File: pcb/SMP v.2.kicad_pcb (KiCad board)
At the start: 2 copper layers, 114.7 x 58.7 mm, 36 parts, among them J1 USB_C_Receptacle_USB2.0, SW1 SW_Push, U1 ATmega32U2-AU, Y1 16MHz

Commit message: latest version
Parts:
- removed C2, C3: 0.1uF, Capacitor_SMD:C_0805_2012Metric
- moved C5 4.04 mm to (53.7, 54.1), turned to 90 degrees
- moved F1 1.74 mm to (54.3, 45.7), turned to 135 degrees
- moved R4 0.57 mm to (63.2, 40.3)
- moved R5 0.43 mm to (58.4, 40.3)
- moved J1 0.20 mm to (60.9, 29.5)
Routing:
- net Net-(R1-Pad2): track 44.8 -> 22.6 mm
- net GND: track 28.6 -> 15.5 mm
- net +5V: track 17.8 -> 13.2 mm
- net GNDPWR: track 1.65 -> 0.00 mm
- net Net-(F1-Pad2): track 22.2 -> 20.9 mm
- net ROW0: track 99.1 -> 98.0 mm, vias 0 -> 5
- net D+: track 13.2 -> 14.2 mm

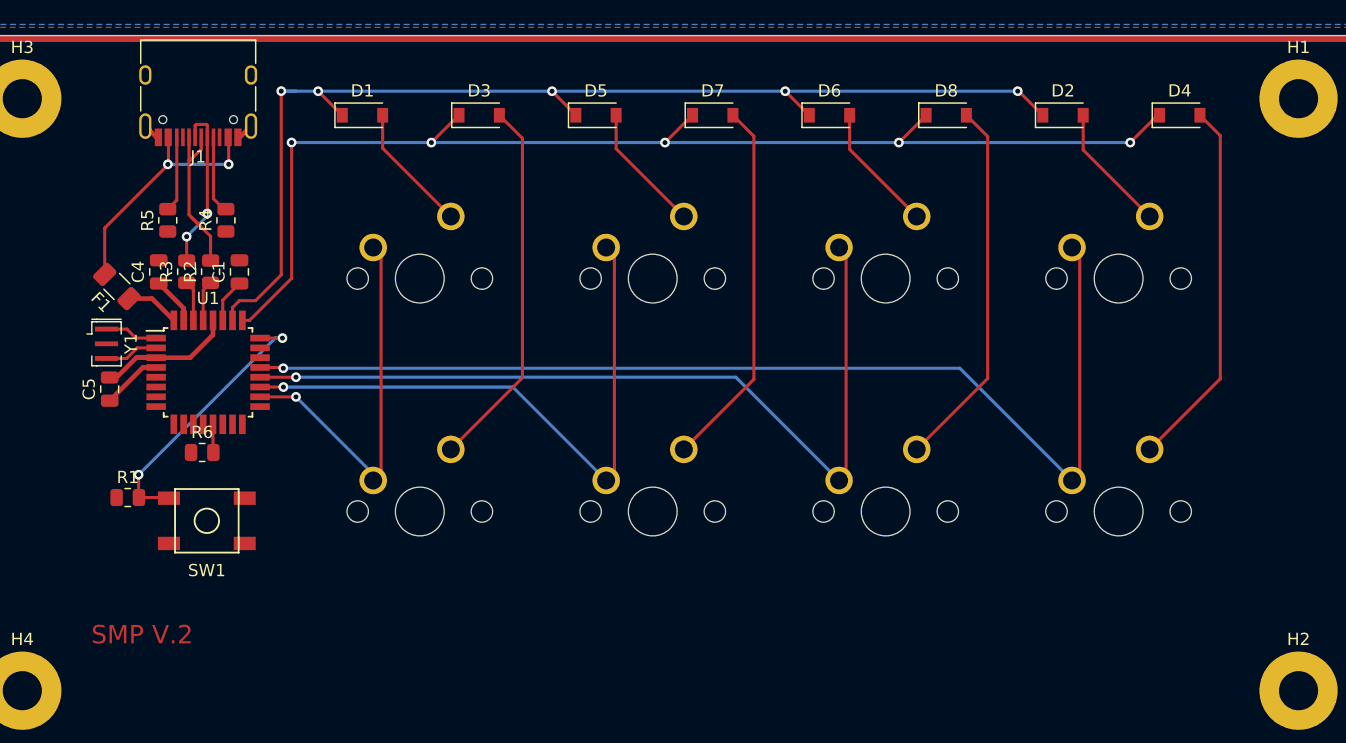
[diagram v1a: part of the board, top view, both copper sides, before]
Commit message: update top plate
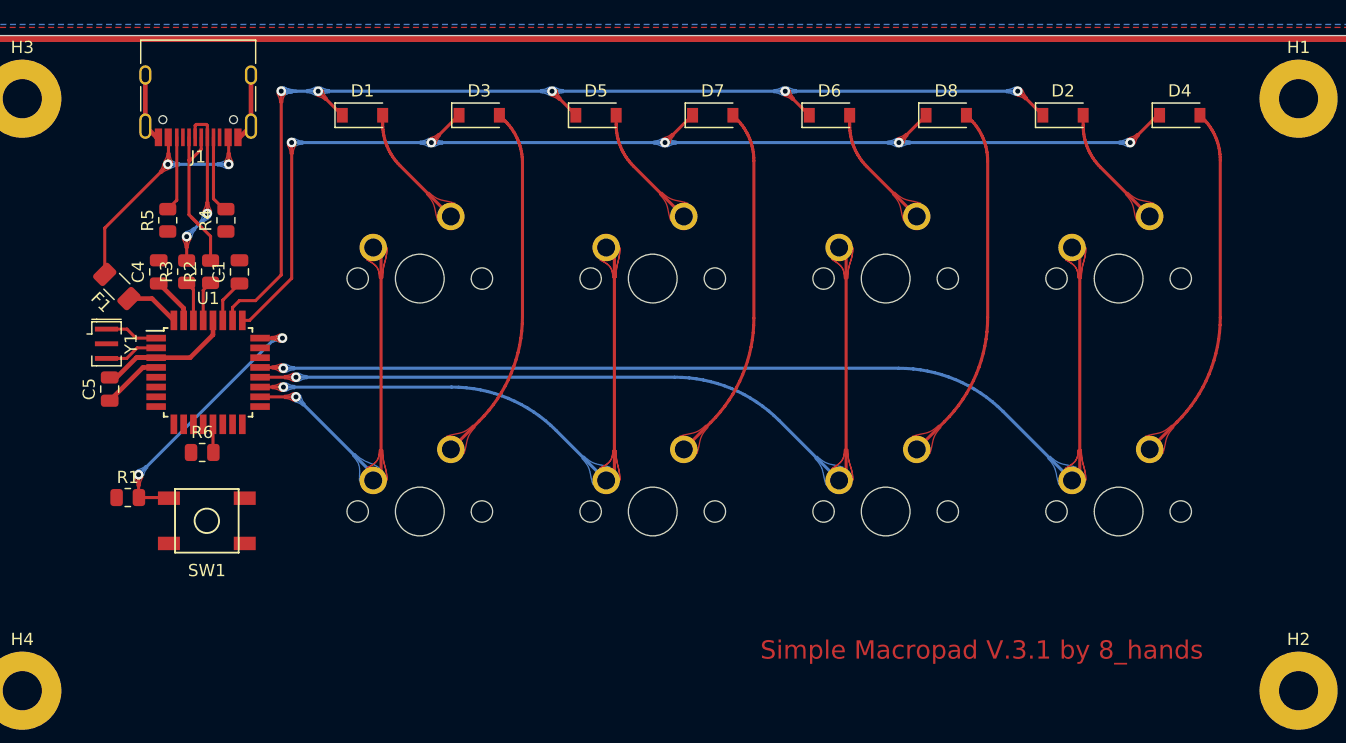
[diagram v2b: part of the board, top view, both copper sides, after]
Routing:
- net GND: track 15.5 -> 23.9 mm
- net Net-(D7-Pad2): track 30.4 -> 29.7 mm
- net Net-(D3-Pad2): track 30.5 -> 29.8 mm
- net Net-(D4-Pad2): track 30.4 -> 29.7 mm
- net Net-(D8-Pad2): track 30.4 -> 29.7 mm
- net COL2: track 70.4 -> 69.9 mm
- net COL1: track 51.1 -> 50.6 mm
- net COL3: track 89.8 -> 89.3 mm
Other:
- board text added: "Simple Macropad V.3.1 by 8_hands"
- board text removed: "SMP V.2"

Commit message: refine the routing
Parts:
- removed J1: USB_C_Receptacle_USB2.0, Connector_USB:USB_C_Receptacle_HRO_TYPE-C-31-M-12
- added C2: 0.1uF, Capacitor_SMD:C_0805_2012Metric, F.Cu at (53.4, 47.1)
- added D9: PRTR5V0U2X, Package_TO_SOT_SMD:SOT-143, F.Cu at (61.0, 39.5)
- added R7: 22, Resistor_SMD:R_0805_2012Metric, F.Cu at (57.7, 39.5)
- added R8: 5.1k, Resistor_SMD:R_0805_2012Metric, F.Cu at (54.8, 36.2)
- added USB1: HRO-TYPE-C-31-M-12, Type-C:HRO-TYPE-C-31-M-12-Assembly, F.Cu at (61.0, 25.8)
- R5: value 5.1k -> 22
- moved R6 7.82 mm to (62.4, 67.1), turned to 90 degrees
- moved SW1 7.25 mm to (61.0, 72.1)
- moved R1 6.04 mm to (59.6, 67.1), turned to 270 degrees
- moved R5 5.97 mm to (64.3, 39.5)
- moved R4 5.41 mm to (66.4, 36.0)
- moved F1 3.72 mm to (54.5, 42.0), turned to 90 degrees
- moved Y1 0.79 mm to (53.7, 51.2)
- moved U1 0.75 mm to (61.0, 52.8)
- moved C5 0.49 mm to (53.3, 54.4), turned to 180 degrees
- moved R2 0.15 mm to (62.1, 44.5)
- moved R3 0.09 mm to (59.9, 44.5)
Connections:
- F1 pad 2: Net-(F1-Pad2) -> VCC
- R1 pad 1: GND -> +5V
- R5 pad 1: GND -> D+
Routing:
- net +5V: track 13.2 -> 37.8 mm, vias 0 -> 2
- net Net-(F1-Pad2): track 20.9 -> 0.00 mm, vias 2 -> 0
- net VCC: track 0.00 -> 17.7 mm, vias 0 -> 2
- net Net-(R1-Pad2): track 22.6 -> 33.4 mm
- net D+: track 14.2 -> 4.34 mm
- net Net-(D9-Pad3): track 0.00 -> 9.66 mm
- net D-: track 14.0 -> 4.34 mm, vias 2 -> 0
- net Net-(R6-Pad2): track 2.32 -> 11.7 mm
- net Net-(R8-Pad2): track 0.00 -> 6.64 mm, vias 0 -> 2
- net ROW0: track 98.0 -> 93.2 mm
- net Net-(D9-Pad2): track 6.18 -> 10.5 mm
- net GND: track 23.9 -> 19.7 mm, vias 0 -> 1
- net Net-(U1-Pad1): track 4.36 -> 3.01 mm
- net ROW1: track 93.8 -> 92.8 mm
- net COL2: track 69.9 -> 70.6 mm
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
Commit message: update firmware
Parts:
- removed C1: 1uF, Capacitor_SMD:C_0805_2012Metric
- removed C2, C4: 0.1uF, Capacitor_SMD:C_0805_2012Metric
- removed C5: 10uF, Capacitor_SMD:C_0805_2012Metric
- removed D9: PRTR5V0U2X, Package_TO_SOT_SMD:SOT-143
- removed F1: 500mA, Fuse:Fuse_1206_3216Metric
- removed R1, R6: 10k, Resistor_SMD:R_0805_2012Metric
- removed R2, R3, R5, R7: 22, Resistor_SMD:R_0805_2012Metric
- removed R4, R8: 5.1k, Resistor_SMD:R_0805_2012Metric
- removed SW1: SW_Push, random-keyboard-parts:SKQG-1155865
- removed USB1: HRO-TYPE-C-31-M-12, Type-C:HRO-TYPE-C-31-M-12-Assembly
- removed Y1: 16MHz, Crystal:Resonator_SMD_muRata_CSTxExxV-3Pin_3.0x1.1mm
- U1: value ATmega32U2-AU -> Elite-C-keebio_without_bottom_row; footprint Package_QFP:TQFP-32_7x7mm_P0.8mm -> Keebio-Parts:Elite-C-ZigZag
- moved U1 8.06 mm to (60.3, 44.7), turned to 270 degrees
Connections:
- U1 pad 13: Net-(R6-Pad2) -> COL0
- U1 pad 14: Net-(U1-Pad14) -> COL1
- U1 pad 15: Net-(U1-Pad15) -> COL2
- U1 pad 16: Net-(U1-Pad16) -> COL3
- U1 pad 18: COL0 -> ROW0
- U1 pad 19: COL1 -> ROW1
- U1 pad 20: COL2 -> Net-(U1-Pad20)
- U1 pad 21: COL3 -> Net-(U1-Pad21)
- U1 pad 25: ROW0 -> (no net)
- U1 pad 26: ROW1 -> (no net)
- U1 pad 27: Net-(C1-Pad1) -> (no net)
- U1 pad 28: GND -> (no net)
- U1 pad 29: Net-(R2-Pad1) -> (no net)
- U1 pad 4: +5V -> GND
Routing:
- net +5V: track 37.8 -> 0.00 mm, vias 2 -> 0
- net Net-(U1-Pad24): track 33.4 -> 0.00 mm, vias 2 -> 0
- net GND: track 19.7 -> 0.00 mm, vias 1 -> 0
- net VCC: track 17.7 -> 0.00 mm, vias 2 -> 0
- net ROW1: track 92.8 -> 80.1 mm, vias 5 -> 4
- net Net-(R6-Pad2): track 11.7 -> 0.00 mm
- net Net-(D9-Pad2): track 10.5 -> 0.00 mm
- net Net-(D9-Pad3): track 9.66 -> 0.00 mm
- net Net-(R8-Pad2): track 6.64 -> 0.00 mm, vias 2 -> 0
- net ROW0: track 93.2 -> 86.9 mm, vias 5 -> 4
- net Net-(R4-Pad2): track 6.01 -> 0.00 mm, vias 2 -> 0
- net D-: track 4.34 -> 0.00 mm
- net D+: track 4.34 -> 0.00 mm
- net COL0: track 32.3 -> 28.2 mm, vias 1 -> 0
- net Net-(C1-Pad1): track 3.89 -> 0.00 mm
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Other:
- board text added: "( Elite-C ver. )"
- board text added: "Simple Macropad ver.2 by 8_hands"
- board text removed: "Simple Macropad V.3.1 by 8_hands"

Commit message: update visual
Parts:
- added REF**: OSHW-Logo_5.7x6mm_Copper, Symbol:OSHW-Logo_5.7x6mm_Copper, F.Cu at (110.4, 78.3)
- added Ref**: Val**, 8hands:smp_logo, F.Cu at (130.8, 77.7)
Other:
- board text removed: "( Elite-C ver. )"
- board text removed: "Simple Macropad ver.2 by 8_hands"

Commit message: pcb and plate finalize for v.4
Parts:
- removed H1: MountingHole_Pad, MountingHole:MountingHole_3.2mm_M3_Pad
- removed REF**: OSHW-Logo_5.7x6mm_Copper, Symbol:OSHW-Logo_5.7x6mm_Copper
- removed Ref**: Val**, 8hands:smp_logo
- added D9: D_Small, 8hands:D_DO-35_SOD27_P5.08mm_Horizontal, F.Cu at (121.1, 119.8)
- added He: MountingHole_Pad, MountingHole:MountingHole_3.2mm_M3_Pad, F.Cu at (110.8, 66.0)
- added MX9: MX-NoLED, MX_Only:MXOnly-1U-NoLED, F.Cu at (183.4, 116.4)
- added kibuzzard-6147B285: G***, label, B.Cu at (183.9, 128.7)
- added kibuzzard-6147B2C4: G***, label, B.Cu at (186.7, 126.7)
- added kibuzzard-6147B3E3: G***, label, B.Cu at (178.7, 123.3)
- D1, D2, D3, D4, D5, D6, D7, D8: footprint Diode_SMD:D_SOD-123 -> 8hands:D_DO-35_SOD27_P5.08mm_Horizontal
- U1: footprint Keebio-Parts:Elite-C-ZigZag -> Keebio-Parts:Elite-C-ZigZag_no-fsilks
- moved H4 159.2 mm to (197.7, 128.5)
- moved H3 117.4 mm to (110.8, 128.6)
- moved D7 93.3 mm to (133.8, 119.8), turned to 225 degrees
- moved MX6 91.5 mm to (183.4, 97.3)
- moved MX5 91.5 mm to (164.3, 97.3)
- moved D8 88.3 mm to (127.5, 119.8), turned to 225 degrees
- moved D3 86.8 mm to (128.4, 106.2), turned to 45 degrees
- moved D1 85.2 mm to (115.7, 106.2), turned to 45 degrees
- moved D5 83.6 mm to (121.9, 110.3), turned to 315 degrees
- moved D4 79.6 mm to (128.2, 110.3), turned to 315 degrees
- moved D6 78.6 mm to (115.5, 110.3), turned to 315 degrees
- moved D2 75.1 mm to (122.1, 106.2), turned to 45 degrees
- moved U1 74.3 mm to (124.7, 81.8)
- moved MX1 74.1 mm to (145.3, 78.3)
- moved MX2 74.1 mm to (164.3, 78.3)
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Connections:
- D1 pad 1: ROW1 -> ROW2
- D2 pad 1: ROW1 -> ROW2
- D3 pad 1: ROW0 -> ROW2
- D4 pad 1: ROW0 -> ROW1
- MX2 pad 2: Net-(D5-Pad2) -> Net-(D2-Pad2)
- MX3 pad 2: Net-(D6-Pad2) -> Net-(D3-Pad2)
- MX4 pad 1: COL3 -> COL0
- MX4 pad 2: Net-(D2-Pad2) -> Net-(D4-Pad2)
- MX5 pad 1: COL0 -> COL1
- MX5 pad 2: Net-(D3-Pad2) -> Net-(D5-Pad2)
- MX6 pad 1: COL1 -> COL2
- MX6 pad 2: Net-(D7-Pad2) -> Net-(D6-Pad2)
- MX7 pad 1: COL2 -> COL0
- MX7 pad 2: Net-(D8-Pad2) -> Net-(D7-Pad2)
- MX8 pad 1: COL3 -> COL1
- MX8 pad 2: Net-(D4-Pad2) -> Net-(D8-Pad2)
- U1 pad 10: Net-(U1-Pad10) -> ROW1
- U1 pad 11: Net-(U1-Pad11) -> ROW2
- U1 pad 13: COL0 -> Net-(U1-Pad13)
- U1 pad 14: COL1 -> Net-(U1-Pad14)
- U1 pad 15: COL2 -> Net-(U1-Pad15)
- U1 pad 16: COL3 -> Net-(U1-Pad16)
- U1 pad 18: ROW0 -> Net-(U1-Pad18)
- U1 pad 19: ROW1 -> Net-(U1-Pad19)
- U1 pad 6: Net-(U1-Pad6) -> COL2
- U1 pad 7: Net-(U1-Pad7) -> COL1
- U1 pad 8: Net-(U1-Pad8) -> COL0
- U1 pad 9: Net-(U1-Pad9) -> ROW0
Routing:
- net COL3: track 87.7 -> 0.00 mm
- net Net-(D9-Pad2): track 0.00 -> 82.0 mm
- net COL2: track 68.6 -> 142.2 mm
- net Net-(D6-Pad2): track 10.3 -> 82.0 mm
- net COL1: track 47.5 -> 118.7 mm
- net COL0: track 28.2 -> 97.5 mm
- net Net-(D2-Pad2): track 10.3 -> 57.6 mm
- net Net-(D5-Pad2): track 10.4 -> 56.1 mm
- net ROW1: track 80.1 -> 35.6 mm, vias 4 -> 0
- net Net-(D3-Pad2): track 29.8 -> 71.1 mm
- net ROW0: track 86.5 -> 49.3 mm, vias 4 -> 0
- net Net-(D1-Pad2): track 10.4 -> 45.6 mm
- net ROW2: track 0.00 -> 26.7 mm
- net Net-(D8-Pad2): track 29.7 -> 56.4 mm
- net Net-(D7-Pad2): track 29.7 -> 30.6 mm
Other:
- board size 114.7 x 58.7 mm -> 94.1 x 69.7 mm
- board text added: "Pro Micro ~Elite-c~"
- board text added: "rev.4"

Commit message: last commit
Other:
- net class Default removed
- net class Power removed
- board text added: "Pro Micro ~{Elite-c}"
- board text removed: "Pro Micro ~Elite-c~"
